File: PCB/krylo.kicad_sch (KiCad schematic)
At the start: 51 parts, among them SW1 Switch, SW10 Switch, SW11 Switch, SW12 Switch, SW13 Switch, SW14 Switch, SW15 Switch, SW16 Switch, SW2 Switch, SW3 Switch, SW4 Switch, SW5 Switch, SW6 Switch, SW7 Switch, SW8 Switch, SW9 Switch, U1 nice_nano

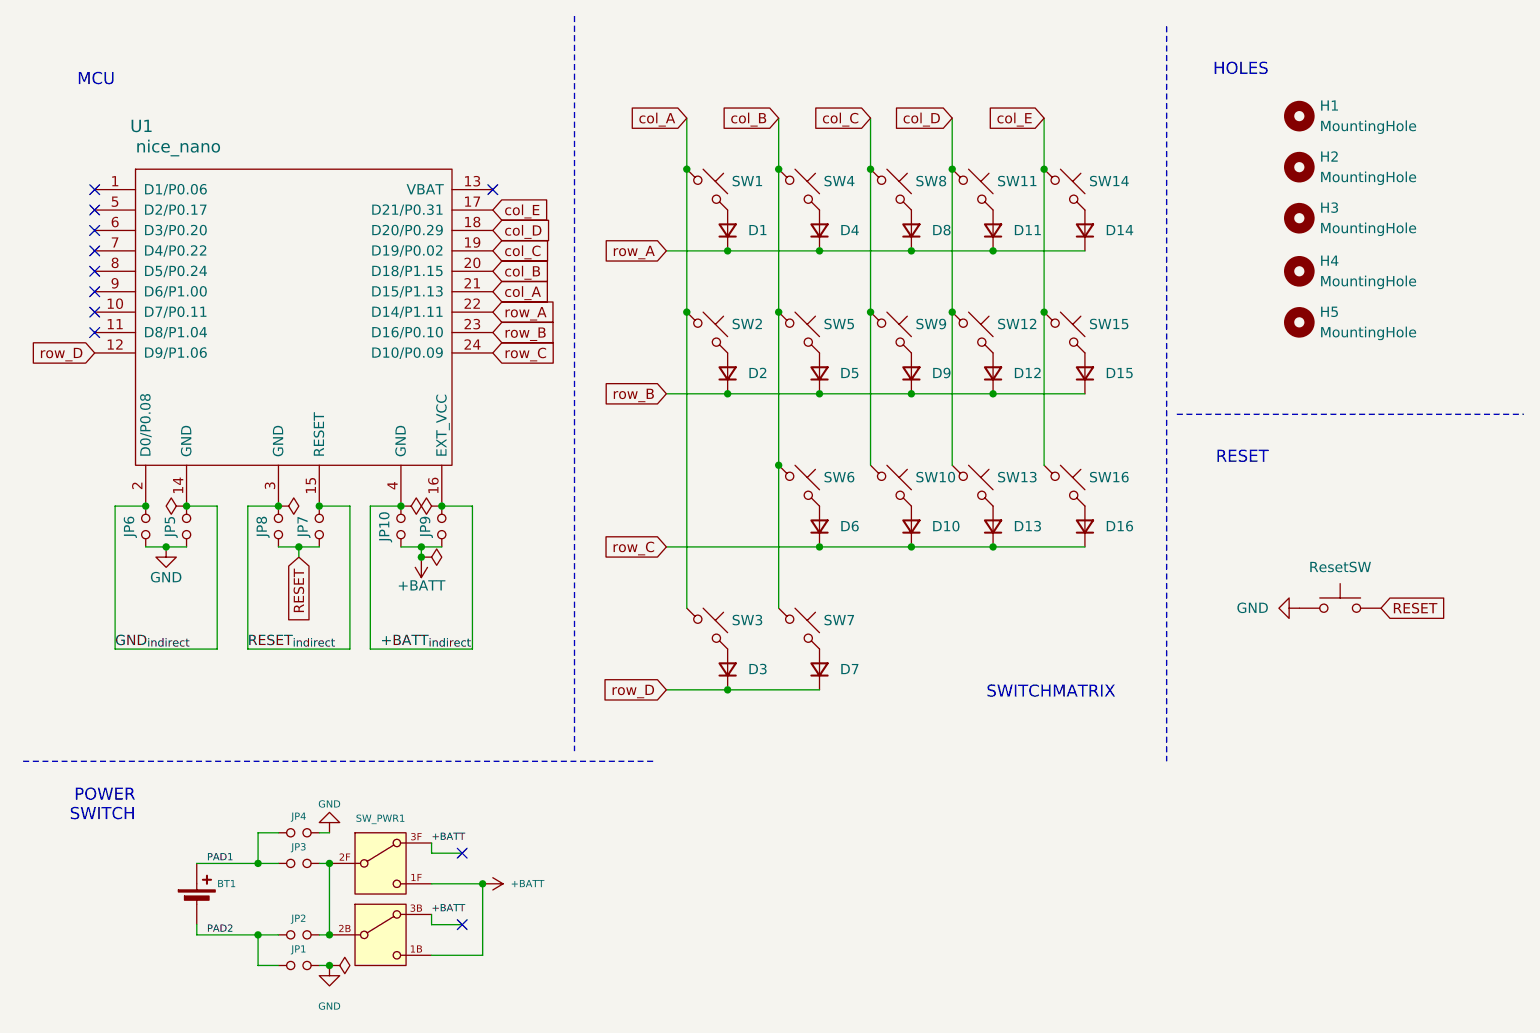
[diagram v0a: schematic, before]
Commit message: JST replaced by Molex, symbols correction and update for the smt_m2 and molex
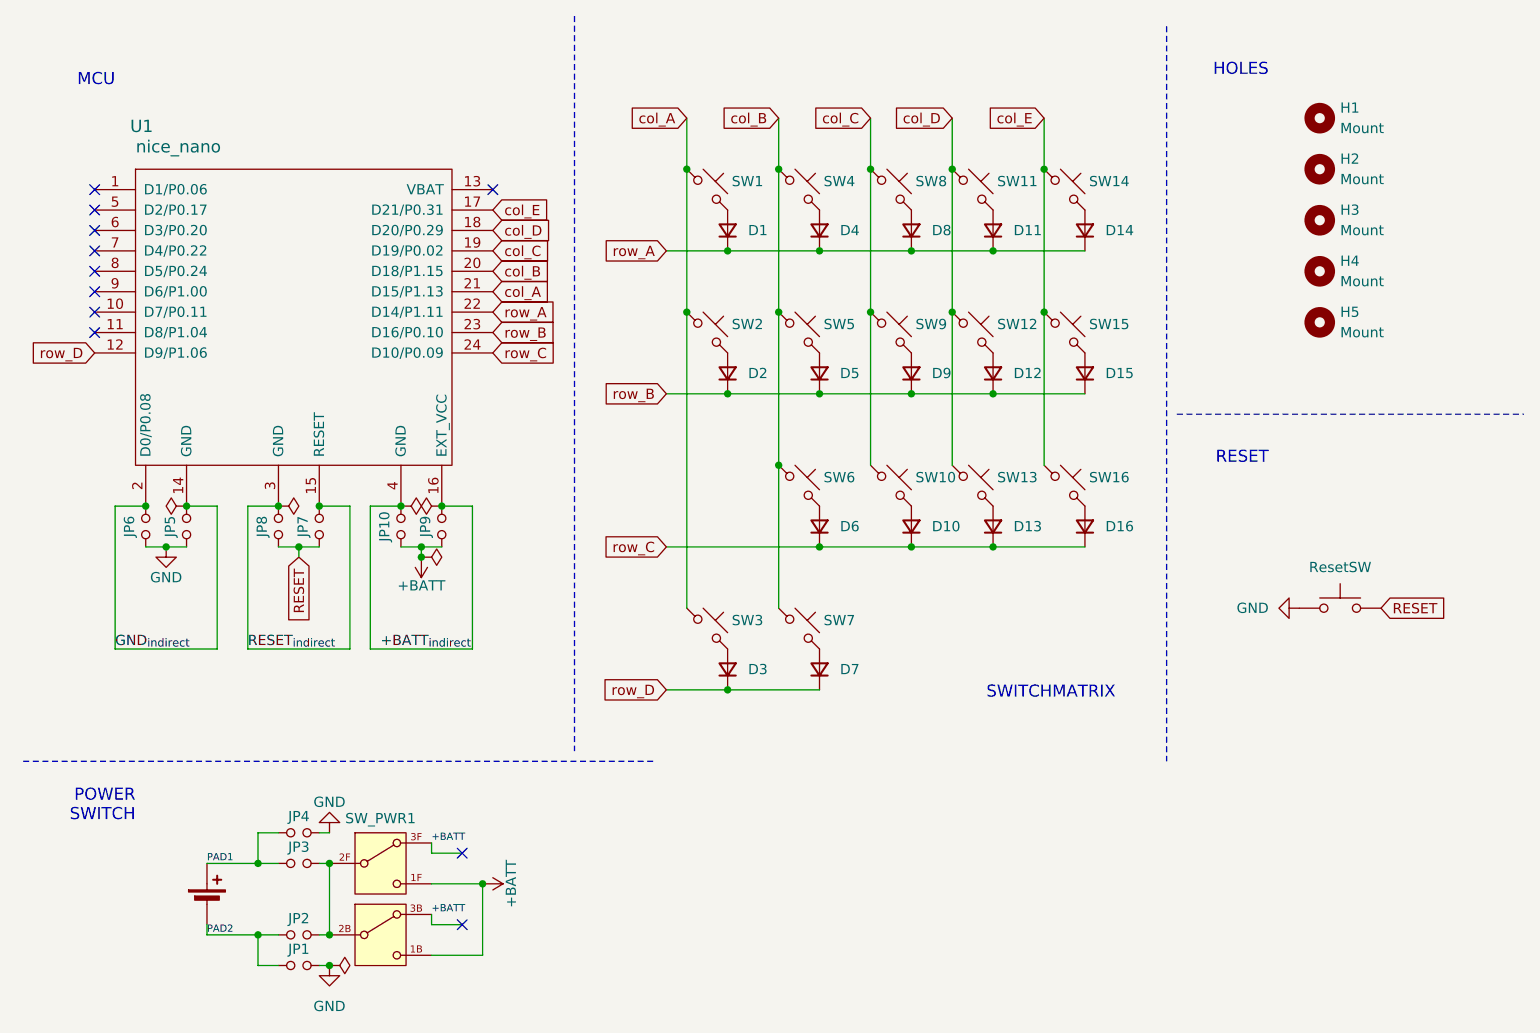
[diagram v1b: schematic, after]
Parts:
- removed BT1: JST_PH, krylo:Molex_connector, symbol krylo:JST_PH
- removed H1, H2, H3, H4, H5: MountingHole, krylo:SMT_M2, symbol krylo:MountingHole
- added BT1: MOLEX_C, krylo:Molex_connector, symbol krylo:MOLEX_C
- added H1, H2, H3, H4, H5: Mount, krylo:SMT_M2, symbol krylo:Mount
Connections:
- net PAD1: now also BT1.1 (+)
- net PAD2: now also BT1.2 (-)

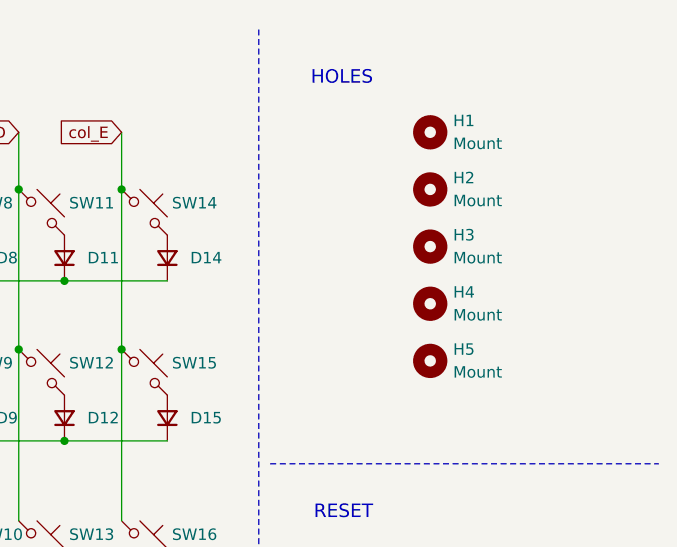
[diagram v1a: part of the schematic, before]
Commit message: Mount points repositioned. Edge cuts revisioned, starting to position the Molex_connector
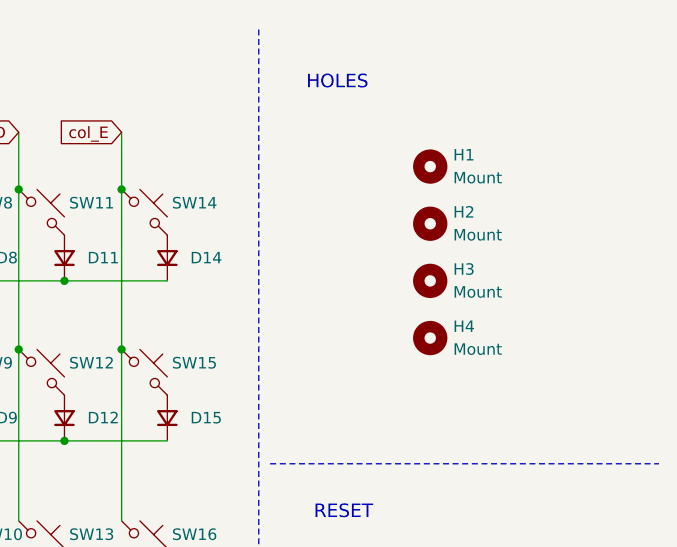
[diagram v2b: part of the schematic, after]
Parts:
- removed H5: Mount, krylo:SMT_M2, symbol krylo:Mount
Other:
- moved on the sheet: H1, H2, H3, H4
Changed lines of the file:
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@@
 	(text "HOLES"
 		(exclude_from_sim no)
-		(at 166.37 19.05 0)
+		(at 165.862 19.558 0)
 		(effects
 			(font
@@
 	(symbol
 		(lib_id "krylo:Mount")
-		(at 172.72 30.48 0)
+		(at 172.72 34.29 0)
 		(unit 1)
 		(body_style 1)
@@
 		(fields_autoplaced yes)
 		(property "Reference" "H2"
-			(at 175.26 29.2099 0)
+			(at 175.26 33.0199 0)
 			(show_name no)
 			(do_not_autoplace no)
@@
 		)
 		(property "Value" "Mount"
-			(at 175.26 31.7499 0)
+			(at 175.26 35.5599 0)
 			(show_name no)
 			(do_not_autoplace no)
@@
 		)
 		(property "Footprint" "krylo:SMT_M2"
-			(at 172.72 30.48 0)
+			(at 172.72 34.29 0)
 			(hide yes)
 			(show_name no)
@@
 		)
 		(property "Datasheet" ""
-			(at 172.72 30.48 0)
+			(at 172.72 34.29 0)
 			(hide yes)
 			(show_name no)
@@
 		)
 		(property "Description" "M2 mounting hole"
-			(at 172.72 30.48 0)
+			(at 172.72 34.29 0)
 			(hide yes)
 			(show_name no)
@@
 	(symbol
 		(lib_id "krylo:Mount")
-		(at 172.72 43.18 0)
+		(at 172.72 46.99 0)
 		(unit 1)
 		(body_style 1)
@@
 		(fields_autoplaced yes)
 		(property "Reference" "H4"
-			(at 175.26 41.9099 0)
+			(at 175.26 45.7199 0)
 			(show_name no)
 			(do_not_autoplace no)
@@
 		)
 		(property "Value" "Mount"
-			(at 175.26 44.4499 0)
+			(at 175.26 48.2599 0)
 			(show_name no)
 			(do_not_autoplace no)
@@
 		)
 		(property "Footprint" "krylo:SMT_M2"
-			(at 172.72 43.18 0)
+			(at 172.72 46.99 0)
 			(hide yes)
 			(show_name no)
@@
 		)
 		(property "Datasheet" ""
-			(at 172.72 43.18 0)
+			(at 172.72 46.99 0)
 			(hide yes)
 			(show_name no)
@@
 		)
 		(property "Description" "M2 mounting hole"
-			(at 172.72 43.18 0)
+			(at 172.72 46.99 0)
 			(hide yes)
 			(show_name no)
@@
 	(symbol
 		(lib_id "krylo:Mount")
-		(at 172.72 36.83 0)
+		(at 172.72 40.64 0)
 		(unit 1)
 		(body_style 1)
@@
 		(fields_autoplaced yes)
 		(property "Reference" "H3"
-			(at 175.26 35.5599 0)
+			(at 175.26 39.3699 0)
 			(show_name no)
 			(do_not_autoplace no)
@@
 		)
 		(property "Value" "Mount"
-			(at 175.26 38.0999 0)
+			(at 175.26 41.9099 0)
 			(show_name no)
 			(do_not_autoplace no)
@@
 		)
 		(property "Footprint" "krylo:SMT_M2"
-			(at 172.72 36.83 0)
+			(at 172.72 40.64 0)
 			(hide yes)
 			(show_name no)
@@
 		)
 		(property "Datasheet" ""
-			(at 172.72 36.83 0)
+			(at 172.72 40.64 0)
 			(hide yes)
 			(show_name no)
@@
 		)
 		(property "Description" "M2 mounting hole"
-			(at 172.72 36.83 0)
+			(at 172.72 40.64 0)
 			(hide yes)
 			(show_name no)
@@
 	)
 	(symbol
-		(lib_id "krylo:Mount")
-		(at 172.72 49.53 0)
-		(unit 1)
-		(body_style 1)
-		(exclude_from_sim no)
-		(in_bom no)
-		(on_board yes)
-		(in_pos_files yes)
-		(dnp no)
-		(fields_autoplaced yes)
-		(property "Reference" "H5"
-			(at 175.26 48.2599 0)
-			(show_name no)
-			(do_not_autoplace no)
-			(effects
-				(font
-					(size 1.27 1.27)
-				)
-				(justify left)
-			)
-		)
-		(property "Value" "Mount"
-			(at 175.26 50.7999 0)
-			(show_name no)
-			(do_not_autoplace no)
-			(effects
-				(font
-					(size 1.27 1.27)
-				)
-				(justify left)
-			)
-		)
-		(property "Footprint" "krylo:SMT_M2"
-			(at 172.72 49.53 0)
-			(hide yes)
-			(show_name no)
-			(do_not_autoplace no)
-			(effects
-				(font
-					(size 1.27 1.27)
-				)
-			)
-		)
-		(property "Datasheet" ""
-			(at 172.72 49.53 0)
-			(hide yes)
-			(show_name no)
-			(do_not_autoplace no)
-			(effects
-				(font
-					(size 1.27 1.27)
-				)
-			)
-		)
-		(property "Description" "M2 mounting hole"
-			(at 172.72 49.53 0)
-			(hide yes)
-			(show_name no)
-			(do_not_autoplace no)
-			(effects
-				(font
-					(size 1.27 1.27)
-				)
-			)
-		)
-		(instances
-			(project "krylo"
-				(path "/231ead31-262f-44fe-a25c-f58d2465dcca"
-					(reference "H5")
-					(unit 1)
-				)
-			)
-		)
-	)
-	(symbol
 		(lib_id "krylo:D_SOD123")
 		(at 132.08 38.1 90)
@@
 	(symbol
 		(lib_id "krylo:Mount")
-		(at 172.72 24.13 0)
+		(at 172.72 27.94 0)
 		(unit 1)
 		(body_style 1)
@@
 		(fields_autoplaced yes)
 		(property "Reference" "H1"
-			(at 175.26 22.8599 0)
+			(at 175.26 26.6699 0)
 			(show_name no)
 			(do_not_autoplace no)
@@
 		)
 		(property "Value" "Mount"
-			(at 175.26 25.3999 0)
+			(at 175.26 29.2099 0)
 			(show_name no)
 			(do_not_autoplace no)
@@
 		)
 		(property "Footprint" "krylo:SMT_M2"
-			(at 172.72 24.13 0)
+			(at 172.72 27.94 0)
 			(hide yes)
 			(show_name no)
@@
 		)
 		(property "Datasheet" ""
-			(at 172.72 24.13 0)
+			(at 172.72 27.94 0)
 			(hide yes)
 			(show_name no)
@@
 		)
 		(property "Description" "M2 mounting hole"
-			(at 172.72 24.13 0)
+			(at 172.72 27.94 0)
 			(hide yes)
 			(show_name no)
